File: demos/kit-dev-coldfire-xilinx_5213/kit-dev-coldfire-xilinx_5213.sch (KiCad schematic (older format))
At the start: 68 parts, among them Q1 3906, U1 MCF5213-LQFP100, U2 74AHC1G14, Y1 8MHz

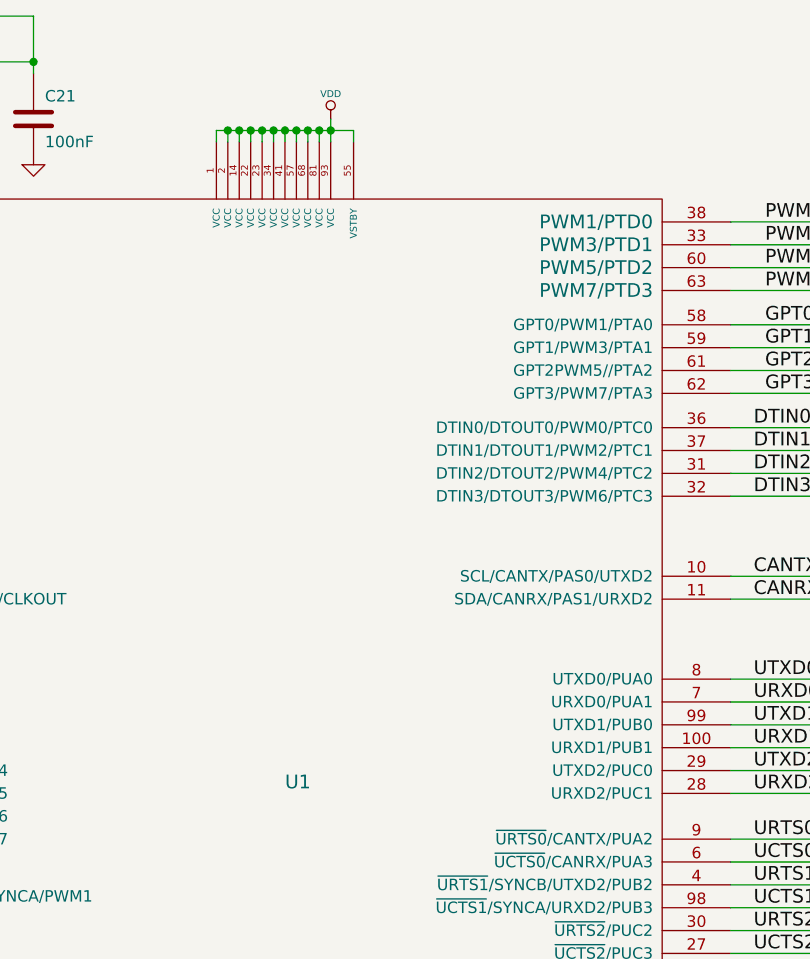
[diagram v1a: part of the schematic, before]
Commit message: add patch from Cirilo Bernardo, and minor fixes.
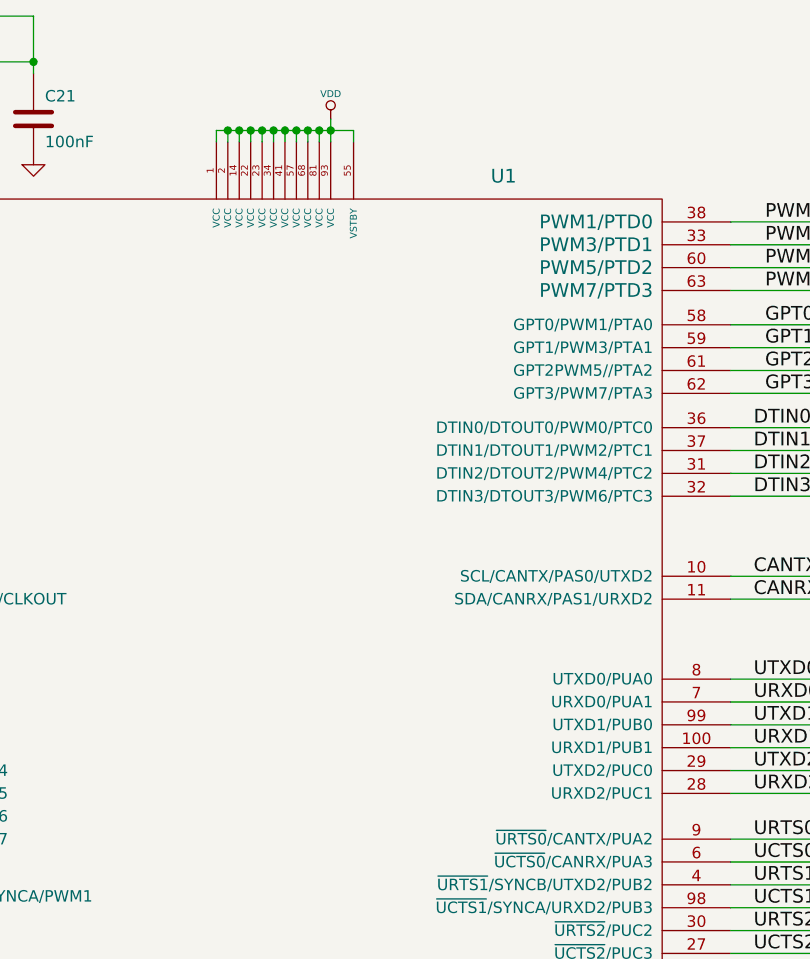
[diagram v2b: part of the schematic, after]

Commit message: 3d viewer: minor code cleaning (remove useless #include ) dialog_track_via_size: set minimal size  and make dialog resizable. Update demo file.
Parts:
- ABRT_SW1, RST_SW1: footprint (none) -> discret:SW_PUSH_SMALL
- ALLPST1, CLKOUT1, GND1, TA-1: footprint (none) -> connect:PINTST
- BDM_EN1, CLK0, CLK1, CT1, VDDA1: footprint (none) -> pin_array:PIN_ARRAY_2X1
- BDM_PORT1: footprint (none) -> pin_array:pin_array_13x2
- C1, C10, C11, C12, C14, C15, C18, C2, C20, C21, C3, C4, C5, C6, C7, C8, C9, R1, R10, R11, R12, R13, R14, R15, R16, R17, R18, R19, R2, R20, R21, R22, R25, R26, R4, R45, R46, R5, R6, R7, R8, R9: footprint (none) -> lib_smd:SM0805
- C16, C17, LEDABRT1, RED1: footprint (none) -> lib_smd:SM1206POL
- D1, D3: footprint (none) -> lib_smd:ST23AK#1
- FB1, L1, L2: footprint (none) -> lib_smd:SM1206
- LV1: footprint (none) -> discret:TO92-INVERT
- Q1: footprint (none) -> lib_smd:SOT23EBC
- U1: footprint (none) -> lib_smd:VQFP100
- U2: footprint (none) -> lib_smd:SOT353
- Y1: footprint (none) -> discret:HC-18UH

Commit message: Very minor fixes.
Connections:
- wire segments 270 -> 269
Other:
- moved on the sheet: ABRT_SW1, ALLPST1, BDM_PORT1, C14, C15, CLKOUT1, CT1, D1, LEDABRT1, R12, R14, R17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

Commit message: demos/ schematic tidying
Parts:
- R21: value 4,7K -> 4.7K
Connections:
- wire segments 269 -> 373
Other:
- moved on the sheet: ABRT_SW1, BDM_PORT1, C1, C10, C11, C12, C14, C15, C16, C17, C18, C2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
